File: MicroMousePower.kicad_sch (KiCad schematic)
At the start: 90 parts, among them J1 USB_C_Receptacle_PowerOnly_6P, J2 Conn_02x16_Odd_Even, J3 Conn_01x02_Pin, Q1 TIP41C, Q2 TIP41C, Q3 TIP41C, U1 INA219AxDCN, U2 MCP73831-3-MC, U3 CH224K, U4 DRV8833PWPR, U5 DRV8833PWPR, U6 TPS61023DRLR, U7 TPS62743YFPT, U8 AP62300WU

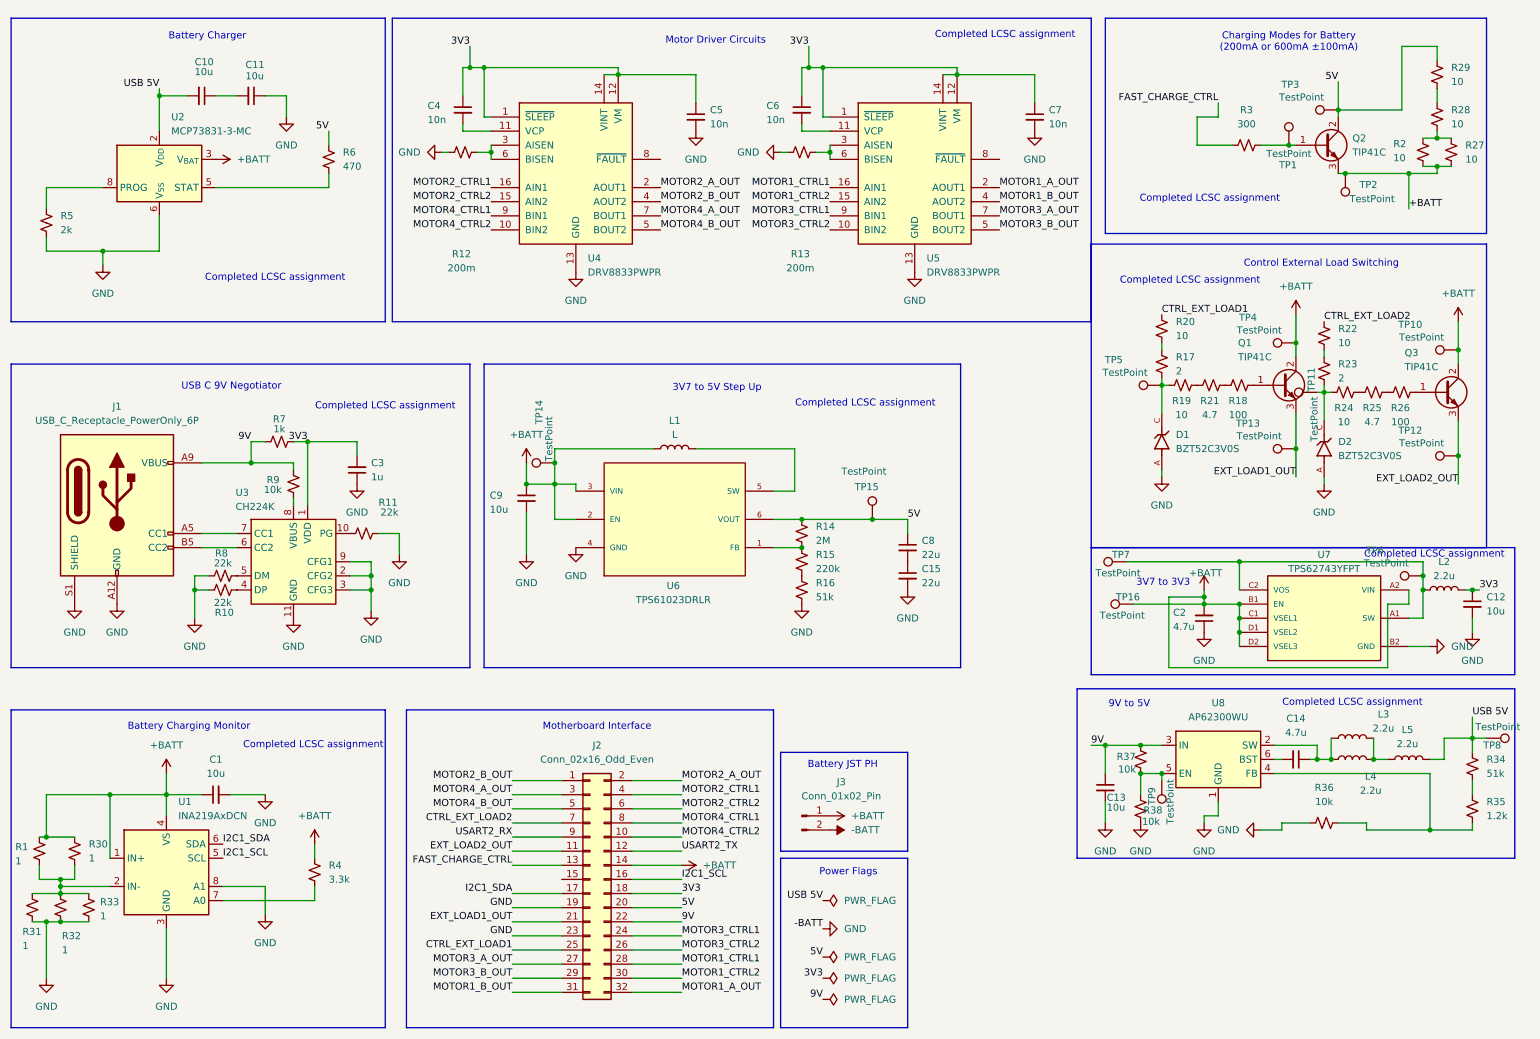
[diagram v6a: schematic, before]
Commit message: added testpoints
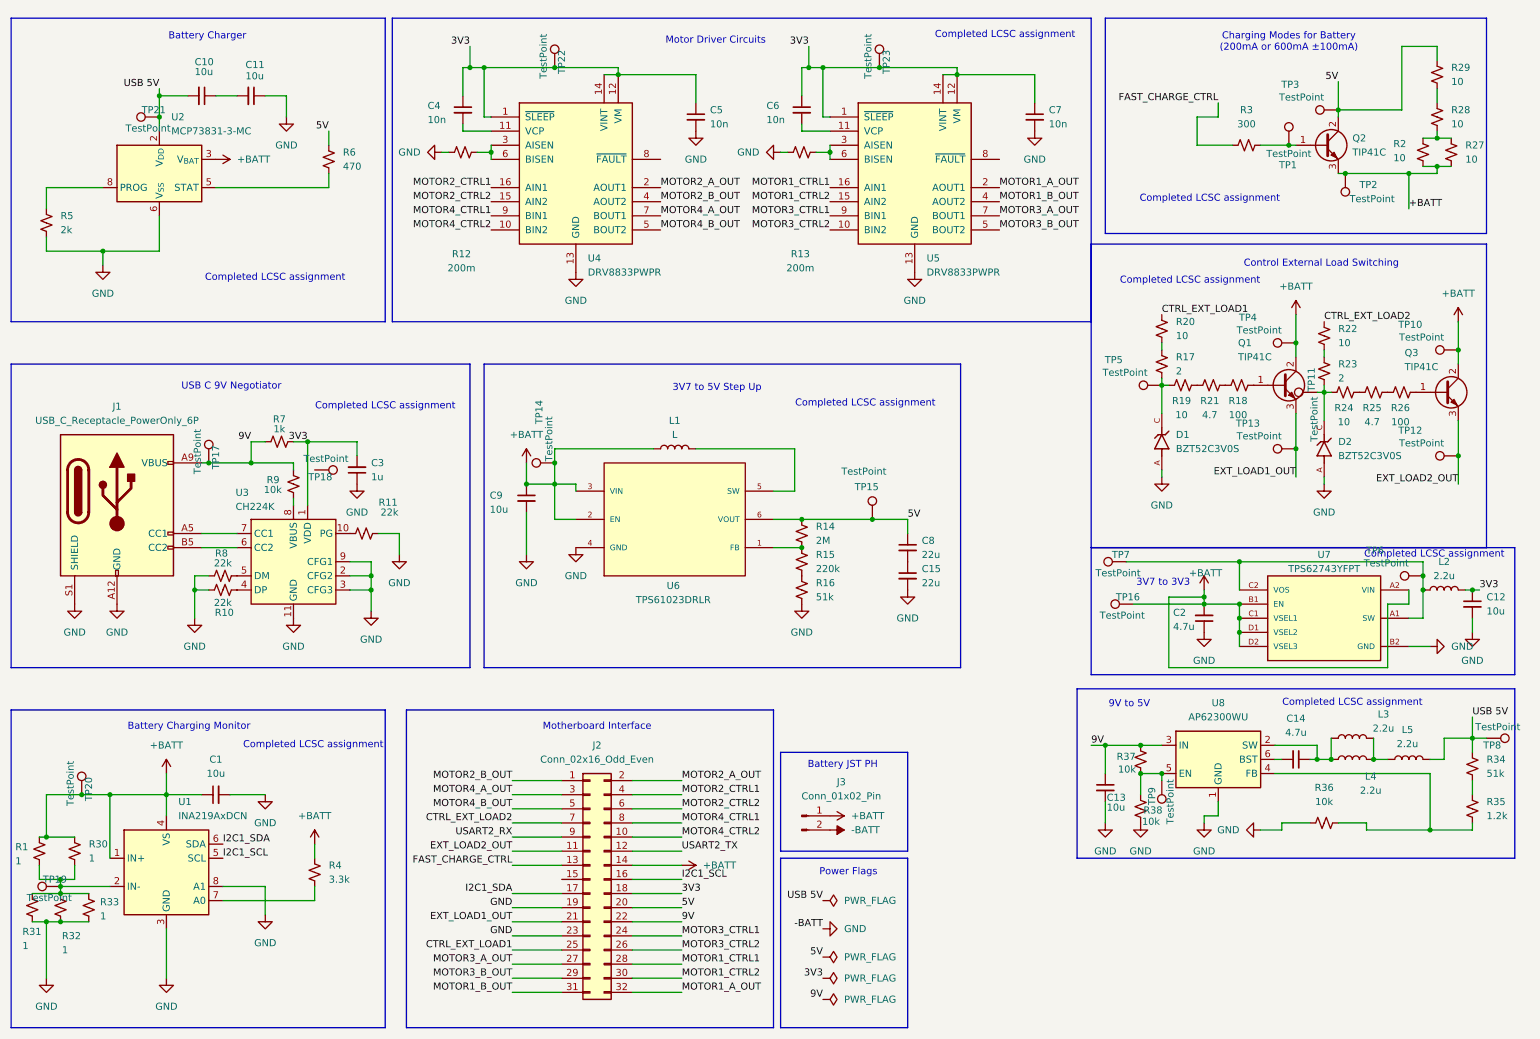
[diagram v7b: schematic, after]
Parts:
- added TP17, TP18, TP19, TP20, TP21, TP22, TP23: TestPoint, symbol Connector:TestPoint
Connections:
- net +BATT: now also TP20.1
- net 3V3: now also TP22.1, TP23.1
- net 9V: now also TP17.1
- net USB 5V: now also TP21.1
- net at R1.2, R30.2, R31.1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: now also TP19.1

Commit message: fixed misc oversights and assigned footprints
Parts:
- added R39, R40, R41, R42, R43, R44: 1, Resistor_SMD:R_0603_1608Metric, symbol Device:R_Small_US
- C1, C10, C11, C12, C13, C4, C5, C6, C7, C9: footprint (none) -> Capacitor_SMD:C_0805_2012Metric
- C14, C2, C3: footprint (none) -> Capacitor_SMD:C_0402_1005Metric
- C15, C8: footprint (none) -> Capacitor_SMD:C_1206_3216Metric
- D1, D2: footprint BZT52C3V0S:DIO_BZT52C3V0S -> Diode_SMD:D_SOD-323
- J2: LCSC (none) -> C5307343
- J3: footprint (none) -> Connector_JST:JST_PH_B2B-PH-K_1x02_P2.00mm_Vertical; LCSC (none) -> C131337
- L1: value L -> 2.2u; footprint (none) -> Inductor_SMD:L_Cenker_CKCS4020; LCSC (none) -> C135262
- L2, L3, L4, L5: footprint (none) -> Inductor_SMD:L_Cenker_CKCS4020
- R1, R14, R21, R25, R30, R31, R32, R33: footprint (none) -> Resistor_SMD:R_0603_1608Metric
- R10, R11, R15, R16, R34, R35, R4, R5, R6, R8: footprint (none) -> Resistor_SMD:R_0805_2012Metric
- R12, R13: value 200m -> 1; footprint (none) -> Resistor_SMD:R_0603_1608Metric; LCSC (none) -> C22936
- R17, R23: footprint (none) -> Resistor_SMD:R_0201_0603Metric
- R18, R19, R2, R20, R22, R24, R26, R27, R28, R29, R3, R36, R37, R38, R7, R9: footprint (none) -> Resistor_SMD:R_1206_3216Metric
- TP1: footprint TestPoint:TestPoint_2Pads_Pitch2.54mm_Drill0.8mm -> TestPoint:TestPoint_Pad_D1.0mm
- TP10, TP11, TP12, TP13, TP14, TP15, TP16, TP17, TP18, TP19, TP2, TP20, TP21, TP22, TP23, TP3, TP4, TP5, TP6, TP7, TP8, TP9: footprint (none) -> TestPoint:TestPoint_Pad_D1.0mm
- U6: footprint TPS61023DRLR:DRL0006A -> Package_TO_SOT_SMD:SOT-563
- U7: footprint TPS62743YFPT:BGA8N40P2X4_87X156X50 -> Package_BGA:Texas_DSBGA-8_0.705x1.468mm_Layout2x4_P0.4mm
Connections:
- net -BATT: now also R39.1, R40.1, R41.1, R42.1, R43.1, R44.1
- net at R12.2, U4.3 (AISEN), U4.6 (BISEN): now also R39.2, R40.2, R41.2
- net at R13.2, U5.3 (AISEN), U5.6 (BISEN): now also R42.2, R43.2, R44.2
